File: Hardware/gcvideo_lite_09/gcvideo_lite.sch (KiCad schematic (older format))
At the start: 44 parts, among them P1 CONN_11X2, P2 CONN_5, P3 CONN_4, P4 CONN_6, P5 CONN_2X2, P6 CONN_1, P7 CONN_1, P8 CONN_1, P9 CONN_1, U1 MachXO2-256-TQ100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

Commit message: update kicad files and replace cdk3404 with adv1725
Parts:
- removed C22: 10u, symbol C
- removed P5: CONN_2X2, symbol CONN_2X2
- removed P6, P7, P8, P9: CONN_1, symbol CONN_1
- removed U2: CDK3404, symbol CDK3404
- added C22, C24: 10n, Capacitor_SMD:C_0603_1608Metric_Pad1.05x0.95mm_HandSolder, symbol gcvideo_lite-rescue:C
- added C23: 100n, Capacitor_SMD:C_0603_1608Metric_Pad1.05x0.95mm_HandSolder, symbol gcvideo_lite-rescue:C
- added C25: 4.7u, Capacitor_SMD:C_0805_2012Metric_Pad1.15x1.40mm_HandSolder, symbol gcvideo_lite-rescue:C
- added U2: ADV7125BCPZ170-RL, Package_QFP:LQFP-48_7x7mm_P0.5mm, symbol eec:ADV7125BCPZ170-RL
- C1, C10, C11, C12, C13, C14, C15, C16, C17, C18, C19, C2, C20, C21, C3, C4, C5, C7, C8, C9: footprint (none) -> Capacitor_SMD:C_0603_1608Metric_Pad1.05x0.95mm_HandSolder; symbol C -> gcvideo_lite-rescue:C
- C6: footprint (none) -> Capacitor_SMD:C_1206_3216Metric_Pad1.33x1.80mm_HandSolder; symbol CP1 -> gcvideo_lite-rescue:CP1
- JP1: footprint (none) -> SOLDER_JUMPER:SOLDER_JUMPER; symbol JUMPER -> gcvideo_lite-rescue:JUMPER
- L1: footprint (none) -> Inductor_SMD:L_0805_2012Metric_Pad1.05x1.20mm_HandSolder; symbol INDUCTOR -> gcvideo_lite-rescue:INDUCTOR
- P1: symbol CONN_11X2 -> conn_11x2:CONN_11X2
- P2: symbol CONN_5 -> gcvideo_lite-rescue:CONN_5
- P3: symbol CONN_4 -> gcvideo_lite-rescue:CONN_4
- P4: symbol CONN_6 -> gcvideo_lite-rescue:CONN_6
- R1, R2, R3, R4, R5, R6, R7, R8: footprint (none) -> Resistor_SMD:R_0805_2012Metric_Pad1.15x1.40mm_HandSolder; symbol R -> gcvideo_lite-rescue:R
- U1: footprint (none) -> Package_QFP:TQFP-100_14x14mm_P0.5mm; symbol MachXO2-256-TQ100 -> machxo2-256-tq100:MachXO2-256-TQ100
- U4: footprint (none) -> Package_SO:SOIC-14_3.9x8.7mm_P1.27mm; symbol 74HC14 -> gcvideo_lite-rescue:74HC14
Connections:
- net labels removed: SPARE1, SPARE2, SPARE3, SPARE4, SPARE5, SPARE6, SPARE7, SPARE8
- wire segments 264 -> 341
- no-connect marks 10 -> 15

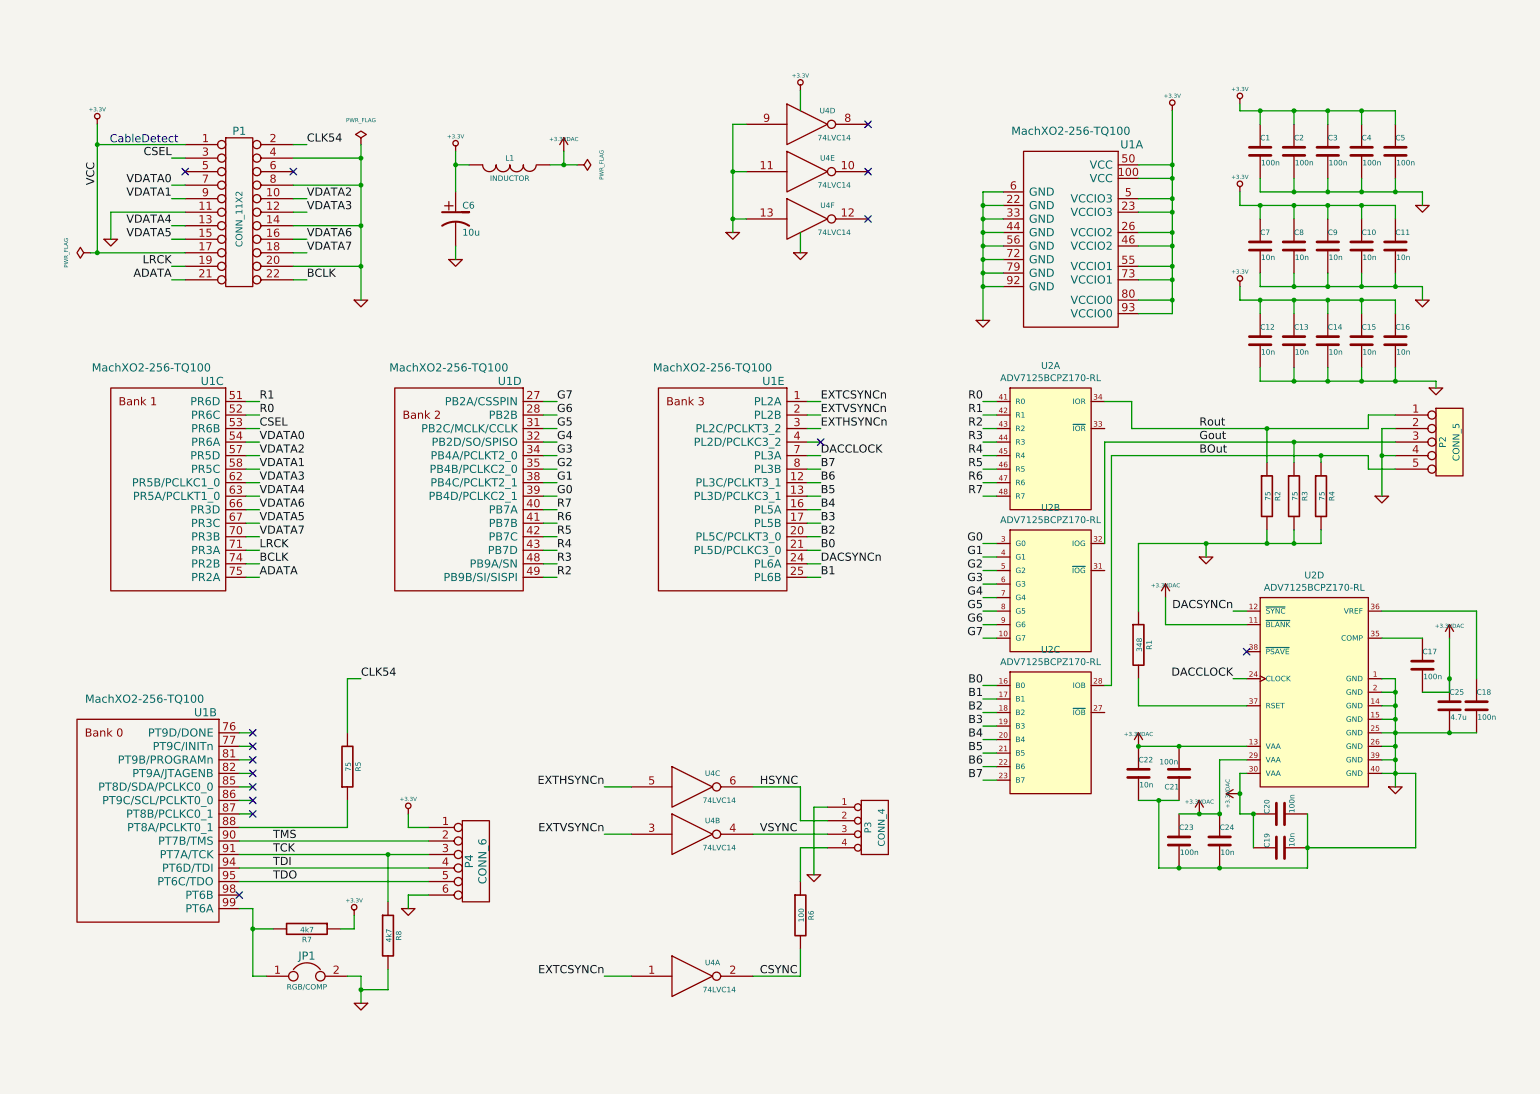
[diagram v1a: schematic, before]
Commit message: updated BOM, redid connectors
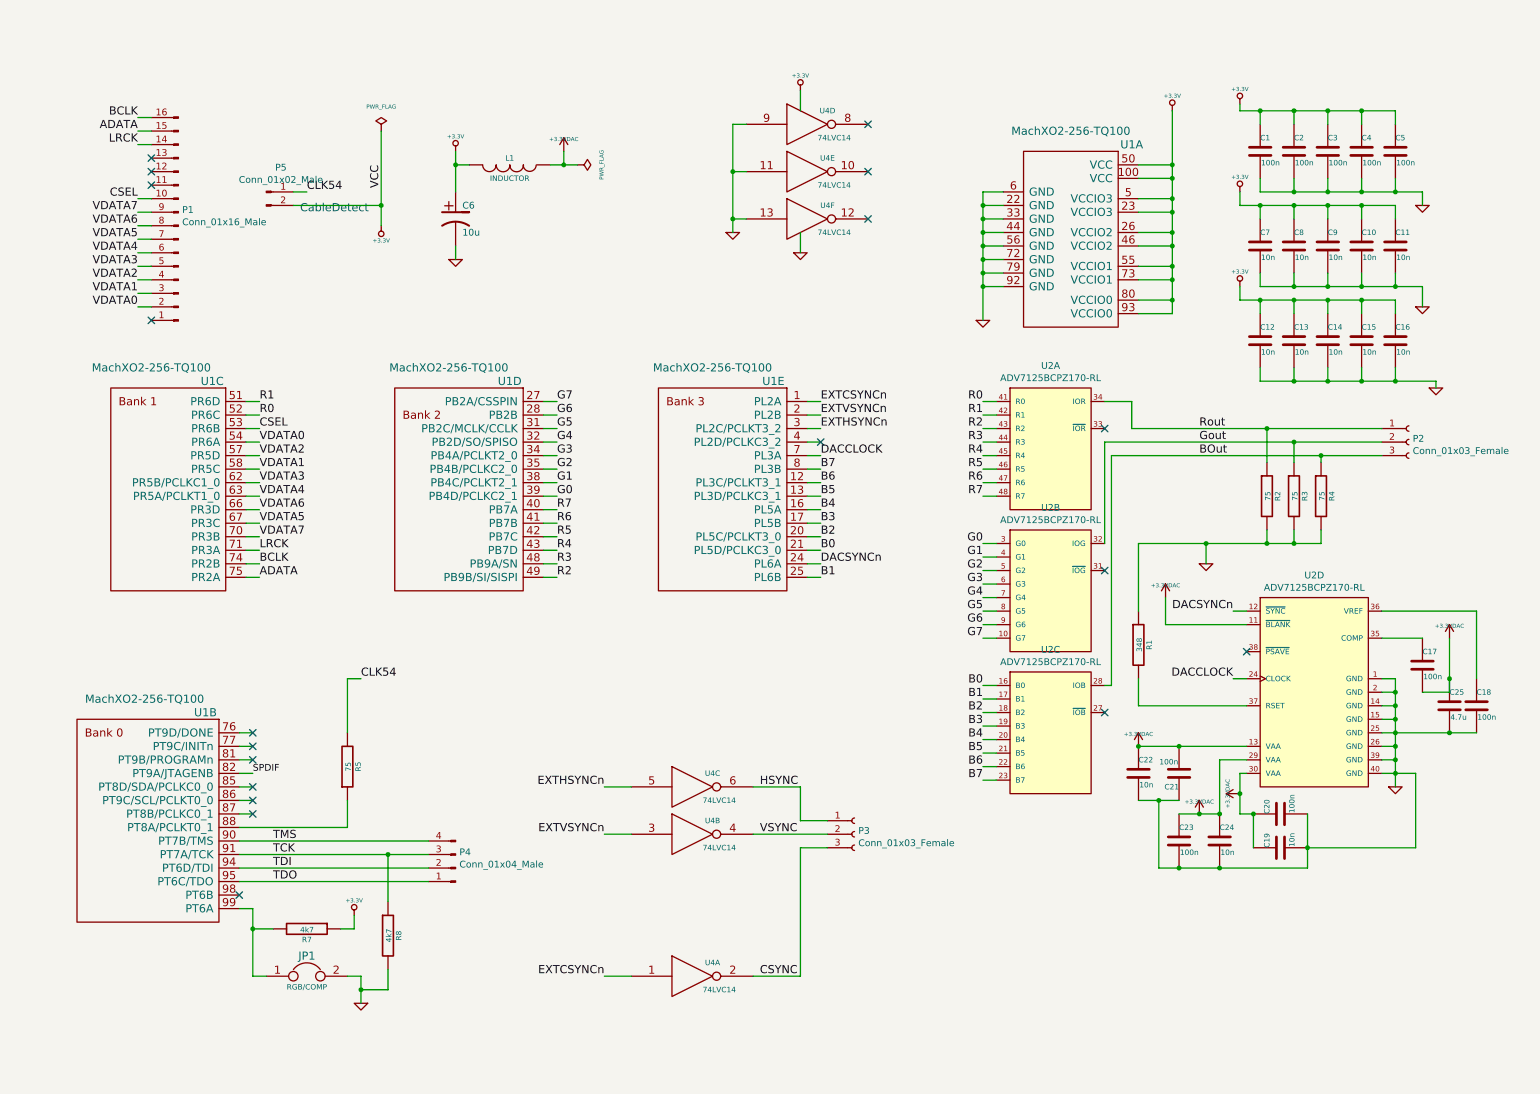
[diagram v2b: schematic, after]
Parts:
- removed P1: CONN_11X2, symbol conn_11x2:CONN_11X2
- removed P2: CONN_5, symbol gcvideo_lite-rescue:CONN_5
- removed P3: CONN_4, symbol gcvideo_lite-rescue:CONN_4
- removed P4: CONN_6, symbol gcvideo_lite-rescue:CONN_6
- removed R6: 100, Resistor_SMD:R_0805_2012Metric_Pad1.15x1.40mm_HandSolder, symbol gcvideo_lite-rescue:R
- added P1: Conn_01x16_Male, symbol Connector:Conn_01x16_Male
- added P2, P3: Conn_01x03_Female, symbol Connector:Conn_01x03_Female
- added P4: Conn_01x04_Male, symbol Connector:Conn_01x04_Male
- added P5: Conn_01x02_Male, symbol Connector:Conn_01x02_Male
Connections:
- net +3.3V: now also P5.2 (Pin_2)
- net ADATA: now also P1.15 (Pin_15)
- net BCLK: now also P1.16 (Pin_16)
- net BOut: now also P2.3 (Pin_3)
- net CLK54: now also P5.1 (Pin_1)
- net CSEL: now also P1.10 (Pin_10)
- net CSYNC: now also P3.3 (Pin_3)
- net Gout: now also P2.2 (Pin_2)
- net HSYNC: now also P3.1 (Pin_1)
- net LRCK: now also P1.14 (Pin_14)
- net Rout: now also P2.1 (Pin_1)
- net TCK: now also P4.3 (Pin_3)
- net TDI: now also P4.2 (Pin_2)
- net TDO: now also P4.1 (Pin_1)
- net TMS: now also P4.4 (Pin_4)
- net VDATA0: now also P1.2 (Pin_2)
- net VDATA1: now also P1.3 (Pin_3)
- net VDATA2: now also P1.4 (Pin_4)
- net VDATA3: now also P1.5 (Pin_5)
- net VDATA4: now also P1.6 (Pin_6)
- net VDATA5: now also P1.7 (Pin_7)
- net VDATA6: now also P1.8 (Pin_8)
- net VDATA7: now also P1.9 (Pin_9)
- net VSYNC: now also P3.2 (Pin_2)
- net SPDIF: now reaches U1.82 (PT9A/JTAGENB)
- no-connect marks 15 -> 19

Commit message: fully updated BOM
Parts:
- removed U4: 74LVC14, Package_SO:SOIC-14_3.9x8.7mm_P1.27mm, symbol gcvideo_lite-rescue:74HC14
- added P6: Conn_01x01_Female, symbol Connector:Conn_01x01_Female
- C25: value 4.7u -> 10u
- C6: footprint Capacitor_SMD:C_1206_3216Metric_Pad1.33x1.80mm_HandSolder -> Capacitor_SMD:C_0805_2012Metric_Pad1.15x1.40mm_HandSolder
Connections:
- net CSYNC is gone; now on net EXTCSYNCn: P3.3 (Pin_3)
- net HSYNC is gone; now on net EXTHSYNCn: P3.1 (Pin_1)
- net VSYNC is gone; now on net EXTVSYNCn: P3.2 (Pin_2)
- net +3.3VDAC: now also C21.1; no longer C21.2
- net GND: now also C21.2; no longer C21.1
- net SPDIF: now also P6.1 (Pin_1)
- no-connect marks 19 -> 16
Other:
- moved on the sheet: C17, C18, C19, C20, C21, C22, C23, C24, C25, P2, P3, R1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

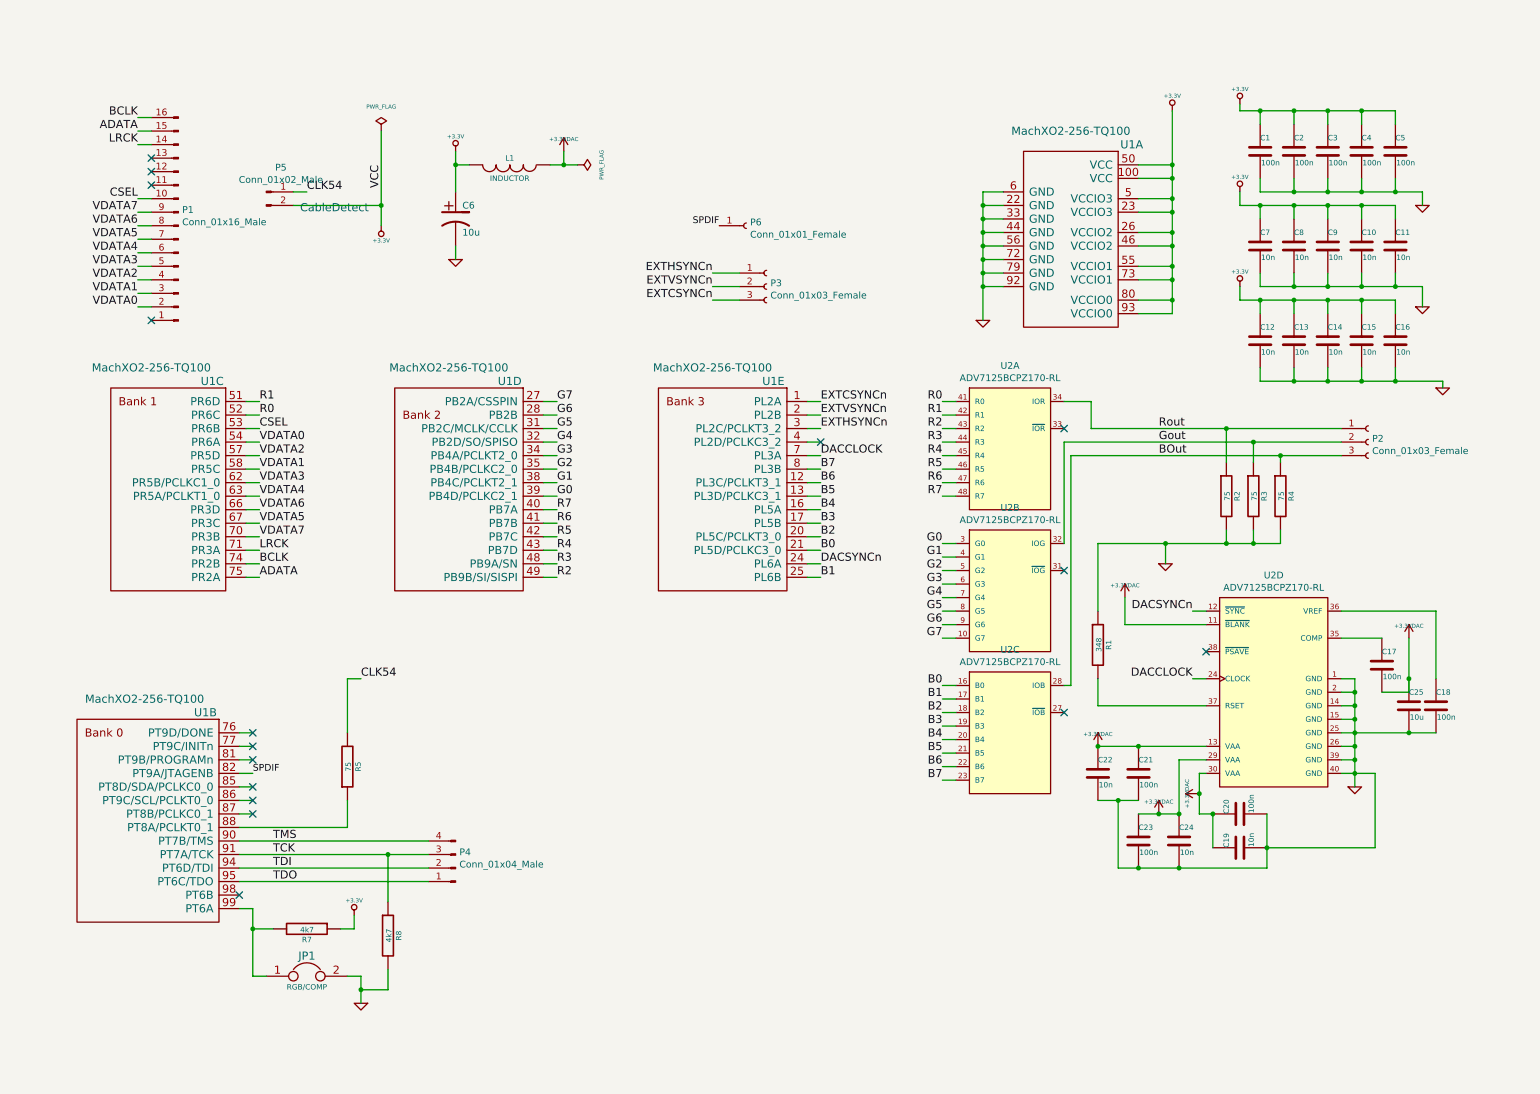
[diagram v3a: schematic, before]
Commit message: update connectors, add footprints
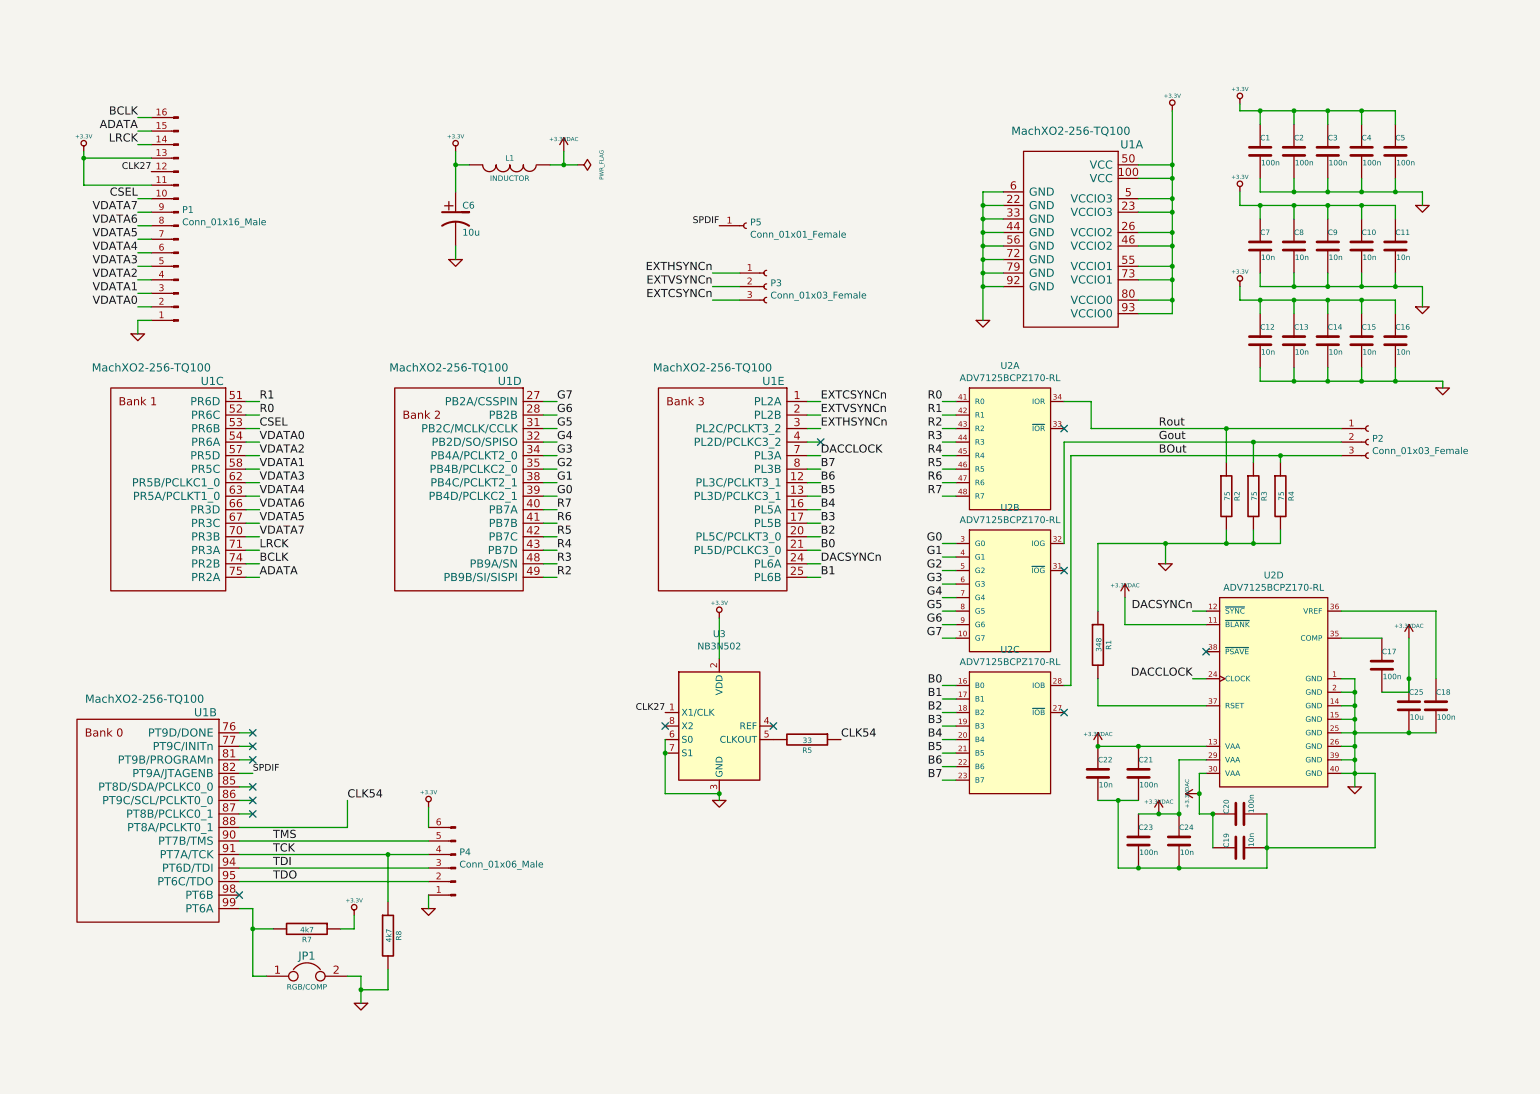
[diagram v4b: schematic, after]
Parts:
- removed P4: Conn_01x04_Male, symbol Connector:Conn_01x04_Male
- removed P5: Conn_01x02_Male, symbol Connector:Conn_01x02_Male
- added P4: Conn_01x06_Male, pads:jtag, symbol Connector:Conn_01x06_Male
- added U3: NB3N502, Package_SO:SOIC-8_3.9x4.9mm_P1.27mm, symbol Oscillator:NB3N502
- P1: footprint (none) -> pads:DOL
- P2: footprint (none) -> pads:rgb
- P3: footprint (none) -> pads:sync
- P5: renamed from P6; footprint (none) -> pads:spdif
- R5: value 75 -> 33
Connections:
- net +3.3V: now also P1.11 (Pin_11), P1.13 (Pin_13), P4.6 (Pin_6), U3.2 (VDD)
- net CLK54: now also R5.1, U1.88 (PT8A/PCLKT0_1); no longer R5.2
- net GND: now also P1.1 (Pin_1), P4.1 (Pin_1), U3.3 (GND), U3.6 (S0), U3.7 (S1)
- net TCK: now also P4.4 (Pin_4)
- net TDI: now also P4.3 (Pin_3)
- net TDO: now also P4.2 (Pin_2)
- net TMS: now also P4.5 (Pin_5)
- net CLK27: now reaches P1.12 (Pin_12)
- net CLK27: now also U3.1 (X1/CLK)
- new net: R5.2, U3.5 (CLKOUT)
- no-connect marks 16 -> 14
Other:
- note removed: "CableDetect"
